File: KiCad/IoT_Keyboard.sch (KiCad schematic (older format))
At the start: 3 parts, among them SW1 SW_Push, U1 Elite-C

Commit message: Update IoT_Keyboard.sch
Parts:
- added C?: 10uF, symbol Device:C_Small
- added C? (x3): 0.1uF, symbol Device:C_Small
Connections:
- net +5V: now also U1.21 (VCC), C?.1, C?.1, C?.1, C?.1
- net GND: now also C?.2, C?.2, C?.2, C?.2
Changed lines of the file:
@@
 F1 "KeyMatrix.sch" 50
 $EndSheet
+$Comp
+L power:+5V #PWR?
+U 1 1 6035BBF9
+P 5000 3000
+F 0 "#PWR?" H 5000 2850 50  0001 C CNN
+F 1 "+5V" H 5015 3173 50  0000 C CNN
+F 2 "" H 5000 3000 50  0001 C CNN
+F 3 "" H 5000 3000 50  0001 C CNN
+	1    5000 3000
+	1    0    0    -1
+$EndComp
+Wire Wire Line
+	4200 3350 4850 3350
+Wire Wire Line
+	4850 3350 4850 3000
+Wire Wire Line
+	4850 3000 5000 3000
+$Comp
+L Device:C_Small C?
+U 1 1 6035F335
+P 1900 3950
+F 0 "C?" H 1992 3996 50  0000 L CNN
+F 1 "10uF" H 1992 3905 50  0000 L CNN
+F 2 "" H 1900 3950 50  0001 C CNN
+F 3 "~" H 1900 3950 50  0001 C CNN
+	1    1900 3950
+	1    0    0    -1
+$EndComp
+$Comp
+L Device:C_Small C?
+U 1 1 60360918
+P 1600 3950
+F 0 "C?" H 1692 3996 50  0000 L CNN
+F 1 "0.1uF" H 1692 3905 50  0000 L CNN
+F 2 "" H 1600 3950 50  0001 C CNN
+F 3 "~" H 1600 3950 50  0001 C CNN
+	1    1600 3950
+	1    0    0    -1
+$EndComp
+$Comp
+L Device:C_Small C?
+U 1 1 60360FBB
+P 1300 3950
+F 0 "C?" H 1392 3996 50  0000 L CNN
+F 1 "0.1uF" H 1392 3905 50  0000 L CNN
+F 2 "" H 1300 3950 50  0001 C CNN
+F 3 "~" H 1300 3950 50  0001 C CNN
+	1    1300 3950
+	1    0    0    -1
+$EndComp
+$Comp
+L Device:C_Small C?
+U 1 1 603612C2
+P 1000 3950
+F 0 "C?" H 1092 3996 50  0000 L CNN
+F 1 "0.1uF" H 1092 3905 50  0000 L CNN
+F 2 "" H 1000 3950 50  0001 C CNN
+F 3 "~" H 1000 3950 50  0001 C CNN
+	1    1000 3950
+	1    0    0    -1
+$EndComp
+Wire Wire Line
+	1000 4050 1300 4050
+Wire Wire Line
+	1300 4050 1450 4050
+Connection ~ 1300 4050
+Wire Wire Line
+	1600 4050 1900 4050
+Connection ~ 1600 4050
+Wire Wire Line
+	1900 3850 1900 3800
+Wire Wire Line
+	1900 3800 1600 3800
+Wire Wire Line
+	1600 3800 1600 3850
+Wire Wire Line
+	1600 3800 1450 3800
+Wire Wire Line
+	1300 3800 1300 3850
+Connection ~ 1600 3800
+Wire Wire Line
+	1300 3800 1000 3800
+Wire Wire Line
+	1000 3800 1000 3850
+Connection ~ 1300 3800
+$Comp
+L power:+5V #PWR?
+U 1 1 60364907
+P 1450 3700
+F 0 "#PWR?" H 1450 3550 50  0001 C CNN
+F 1 "+5V" H 1465 3873 50  0000 C CNN
+F 2 "" H 1450 3700 50  0001 C CNN
+F 3 "" H 1450 3700 50  0001 C CNN
+	1    1450 3700
+	1    0    0    -1
+$EndComp
+$Comp
+L power:GND #PWR?
+U 1 1 603653B9
+P 1450 4150
+F 0 "#PWR?" H 1450 3900 50  0001 C CNN
+F 1 "GND" H 1455 3977 50  0000 C CNN
+F 2 "" H 1450 4150 50  0001 C CNN
+F 3 "" H 1450 4150 50  0001 C CNN
+	1    1450 4150
+	1    0    0    -1
+$EndComp
+Wire Wire Line
+	1450 3800 1450 3700
+Connection ~ 1450 3800
+Wire Wire Line
+	1450 3800 1300 3800
+Wire Wire Line
+	1450 4050 1450 4150
+Connection ~ 1450 4050
+Wire Wire Line
+	1450 4050 1600 4050
 $EndSCHEMATC

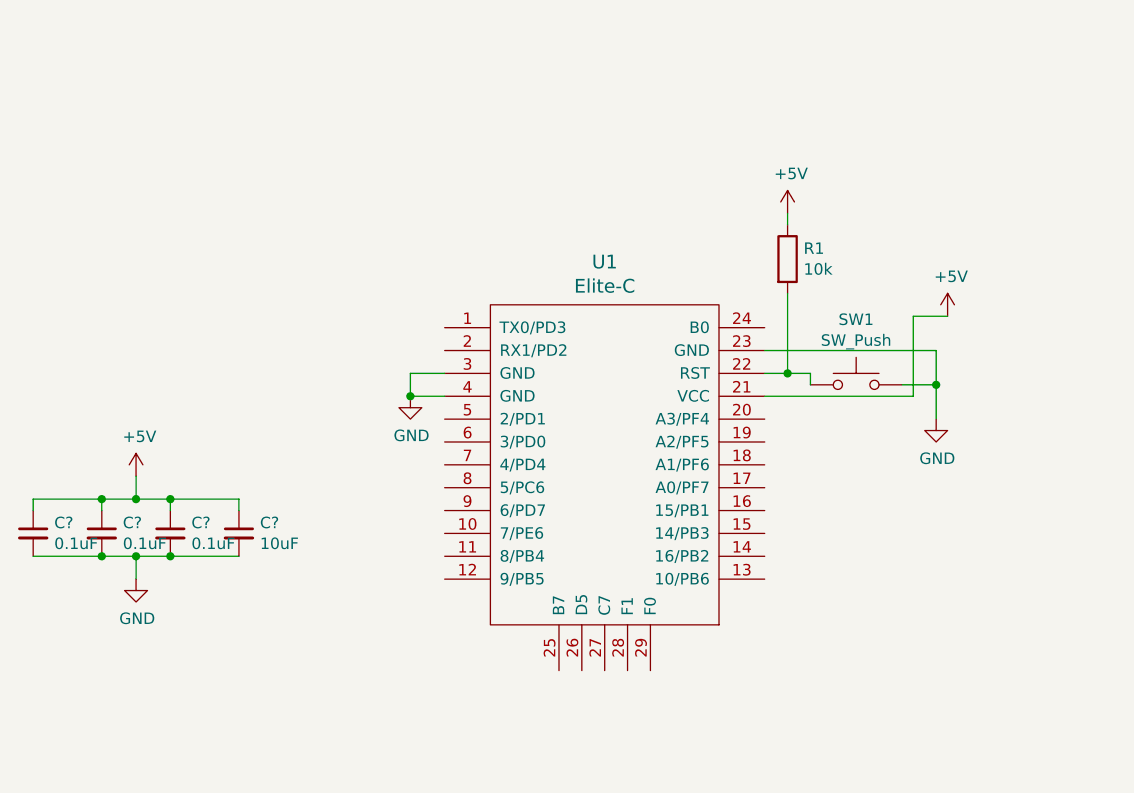
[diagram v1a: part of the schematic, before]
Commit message: Wired Rows/Cols of Switches. Created Physical PCB.
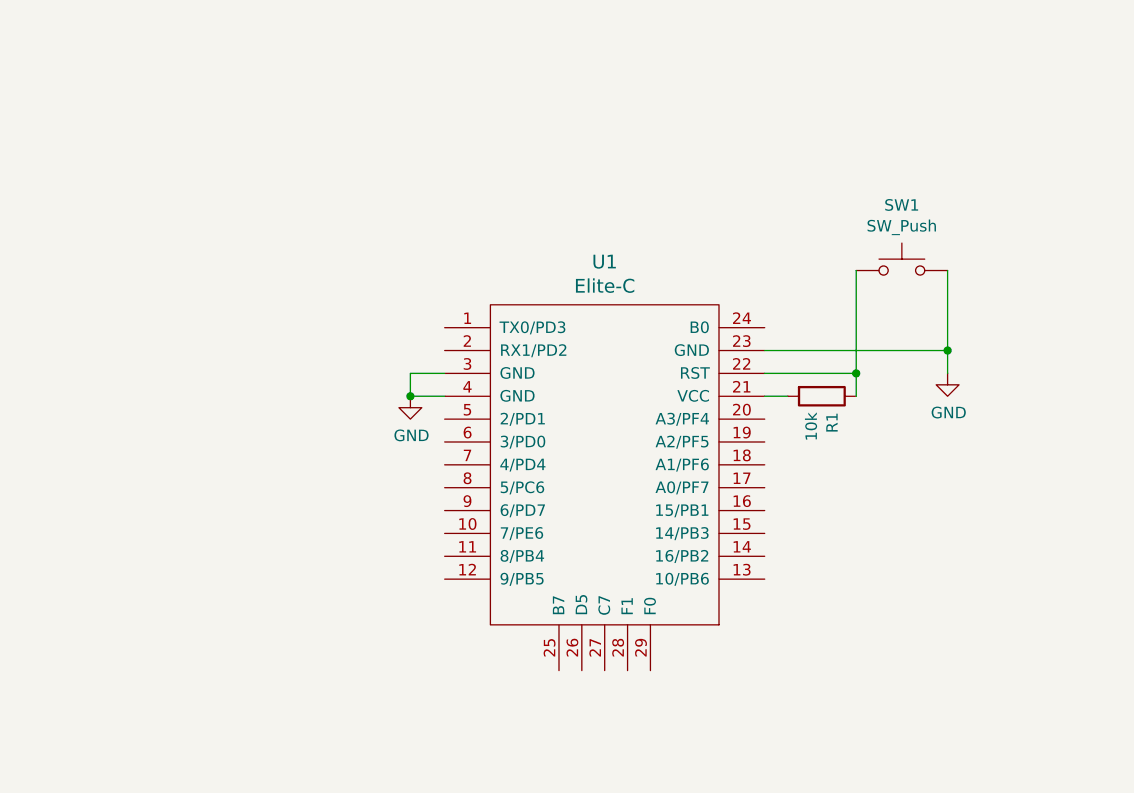
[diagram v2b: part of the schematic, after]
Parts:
- removed C?: 10uF, symbol Device:C_Small
- removed C? (x3): 0.1uF, symbol Device:C_Small
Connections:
- net at SW1.1, U1.22 (RST): now also R1.1; no longer R1.2
- net +5V: no longer names the net of U1.21 (VCC)
- net +5V: now also R1.2; no longer R1.1
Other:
- moved on the sheet: R1, SW1
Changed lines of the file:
@@
 Wire Wire Line
 	2650 3250 2650 3350
-Wire Wire Line
-	4200 3250 4300 3250
-Wire Wire Line
-	4400 3250 4400 3300
 $Comp
 L power:GND #PWR0102
 U 1 1 60210421
-P 4950 3450
-F 0 "#PWR0102" H 4950 3200 50  0001 C CNN
-F 1 "GND" H 4955 3277 50  0000 C CNN
-F 2 "" H 4950 3450 50  0001 C CNN
-F 3 "" H 4950 3450 50  0001 C CNN
-	1    4950 3450
-	1    0    0    -1
-$EndComp
-Wire Wire Line
-	4300 3250 4300 2900
-Connection ~ 4300 3250
-Wire Wire Line
-	4300 3250 4400 3250
-$Comp
-L power:+5V #PWR0103
-U 1 1 602126FC
-P 4300 2550
-F 0 "#PWR0103" H 4300 2400 50  0001 C CNN
-F 1 "+5V" H 4315 2723 50  0000 C CNN
-F 2 "" H 4300 2550 50  0001 C CNN
-F 3 "" H 4300 2550 50  0001 C CNN
-	1    4300 2550
-	1    0    0    -1
-$EndComp
-Wire Wire Line
-	4300 2600 4300 2550
-$Comp
-L Switch:SW_Push SW1
-U 1 1 6020EE71
-P 4600 3300
-F 0 "SW1" H 4600 3585 50  0000 C CNN
-F 1 "SW_Push" H 4600 3494 50  0000 C CNN
-F 2 "Keebio:SW_SPST_3x3" H 4600 3500 50  0001 C CNN
-F 3 "~" H 4600 3500 50  0001 C CNN
-	1    4600 3300
+P 5000 3250
+F 0 "#PWR0102" H 5000 3000 50  0001 C CNN
+F 1 "GND" H 5005 3077 50  0000 C CNN
+F 2 "" H 5000 3250 50  0001 C CNN
+F 3 "" H 5000 3250 50  0001 C CNN
+	1    5000 3250
 	1    0    0    -1
 $EndComp
@@
 L Device:R R1
 U 1 1 60211719
-P 4300 2750
-F 0 "R1" H 4370 2796 50  0000 L CNN
-F 1 "10k" H 4370 2705 50  0000 L CNN
-F 2 "Resistor_SMD:R_0805_2012Metric" V 4230 2750 50  0001 C CNN
-F 3 "~" H 4300 2750 50  0001 C CNN
-	1    4300 2750
-	1    0    0    -1
+P 4450 3350
+F 0 "R1" H 4520 3396 50  0000 L CNN
+F 1 "10k" H 4520 3305 50  0000 L CNN
+F 2 "Resistor_SMD:R_0805_2012Metric" V 4380 3350 50  0001 C CNN
+F 3 "~" H 4450 3350 50  0001 C CNN
+	1    4450 3350
+	0    1    1    0
 $EndComp
 $Comp
@@
 	1    0    0    -1
 $EndComp
-Wire Wire Line
-	4200 3150 4950 3150
-Wire Wire Line
-	4950 3150 4950 3300
-Wire Wire Line
-	4800 3300 4950 3300
-Connection ~ 4950 3300
-Wire Wire Line
-	4950 3300 4950 3450
 $Sheet
 S 12000 0    11700 8250
@@
 $EndSheet
 $Comp
-L power:+5V #PWR?
-U 1 1 6035BBF9
-P 5000 3000
-F 0 "#PWR?" H 5000 2850 50  0001 C CNN
-F 1 "+5V" H 5015 3173 50  0000 C CNN
-F 2 "" H 5000 3000 50  0001 C CNN
-F 3 "" H 5000 3000 50  0001 C CNN
-	1    5000 3000
+L Switch:SW_Push SW1
+U 1 1 6020EE71
+P 4800 2800
+F 0 "SW1" H 4800 3085 50  0000 C CNN
+F 1 "SW_Push" H 4800 2994 50  0000 C CNN
+F 2 "Keebio:SW_SPST_3x3" H 4800 3000 50  0001 C CNN
+F 3 "~" H 4800 3000 50  0001 C CNN
+	1    4800 2800
 	1    0    0    -1
 $EndComp
 Wire Wire Line
-	4200 3350 4850 3350
+	4200 3350 4300 3350
 Wire Wire Line
-	4850 3350 4850 3000
+	4600 3350 4600 3250
 Wire Wire Line
-	4850 3000 5000 3000
-$Comp
-L Device:C_Small C?
-U 1 1 6035F335
-P 1900 3950
-F 0 "C?" H 1992 3996 50  0000 L CNN
-F 1 "10uF" H 1992 3905 50  0000 L CNN
-F 2 "" H 1900 3950 50  0001 C CNN
-F 3 "~" H 1900 3950 50  0001 C CNN
-	1    1900 3950
-	1    0    0    -1
-$EndComp
-$Comp
-L Device:C_Small C?
-U 1 1 60360918
-P 1600 3950
-F 0 "C?" H 1692 3996 50  0000 L CNN
-F 1 "0.1uF" H 1692 3905 50  0000 L CNN
-F 2 "" H 1600 3950 50  0001 C CNN
-F 3 "~" H 1600 3950 50  0001 C CNN
-	1    1600 3950
-	1    0    0    -1
-$EndComp
-$Comp
-L Device:C_Small C?
-U 1 1 60360FBB
-P 1300 3950
-F 0 "C?" H 1392 3996 50  0000 L CNN
-F 1 "0.1uF" H 1392 3905 50  0000 L CNN
-F 2 "" H 1300 3950 50  0001 C CNN
-F 3 "~" H 1300 3950 50  0001 C CNN
-	1    1300 3950
-	1    0    0    -1
-$EndComp
-$Comp
-L Device:C_Small C?
-U 1 1 603612C2
-P 1000 3950
-F 0 "C?" H 1092 3996 50  0000 L CNN
-F 1 "0.1uF" H 1092 3905 50  0000 L CNN
-F 2 "" H 1000 3950 50  0001 C CNN
-F 3 "~" H 1000 3950 50  0001 C CNN
-	1    1000 3950
-	1    0    0    -1
-$EndComp
+	4200 3250 4600 3250
+Connection ~ 4600 3250
+Connection ~ 5000 3150
 Wire Wire Line
-	1000 4050 1300 4050
+	5000 3150 5000 3250
 Wire Wire Line
-	1300 4050 1450 4050
-Connection ~ 1300 4050
+	4200 3150 5000 3150
 Wire Wire Line
-	1600 4050 1900 4050
-Connection ~ 1600 4050
+	5000 2800 5000 3150
 Wire Wire Line
-	1900 3850 1900 3800
-Wire Wire Line
-	1900 3800 1600 3800
-Wire Wire Line
-	1600 3800 1600 3850
-Wire Wire Line
-	1600 3800 1450 3800
-Wire Wire Line
-	1300 3800 1300 3850
-Connection ~ 1600 3800
-Wire Wire Line
-	1300 3800 1000 3800
-Wire Wire Line
-	1000 3800 1000 3850
-Connection ~ 1300 3800
-$Comp
-L power:+5V #PWR?
-U 1 1 60364907
-P 1450 3700
-F 0 "#PWR?" H 1450 3550 50  0001 C CNN
-F 1 "+5V" H 1465 3873 50  0000 C CNN
-F 2 "" H 1450 3700 50  0001 C CNN
-F 3 "" H 1450 3700 50  0001 C CNN
-	1    1450 3700
-	1    0    0    -1
-$EndComp
-$Comp
-L power:GND #PWR?
-U 1 1 603653B9
-P 1450 4150
-F 0 "#PWR?" H 1450 3900 50  0001 C CNN
-F 1 "GND" H 1455 3977 50  0000 C CNN
-F 2 "" H 1450 4150 50  0001 C CNN
-F 3 "" H 1450 4150 50  0001 C CNN
-	1    1450 4150
-	1    0    0    -1
-$EndComp
-Wire Wire Line
-	1450 3800 1450 3700
-Connection ~ 1450 3800
-Wire Wire Line
-	1450 3800 1300 3800
-Wire Wire Line
-	1450 4050 1450 4150
-Connection ~ 1450 4050
-Wire Wire Line
-	1450 4050 1600 4050
+	4600 3250 4600 2800
 $EndSCHEMATC

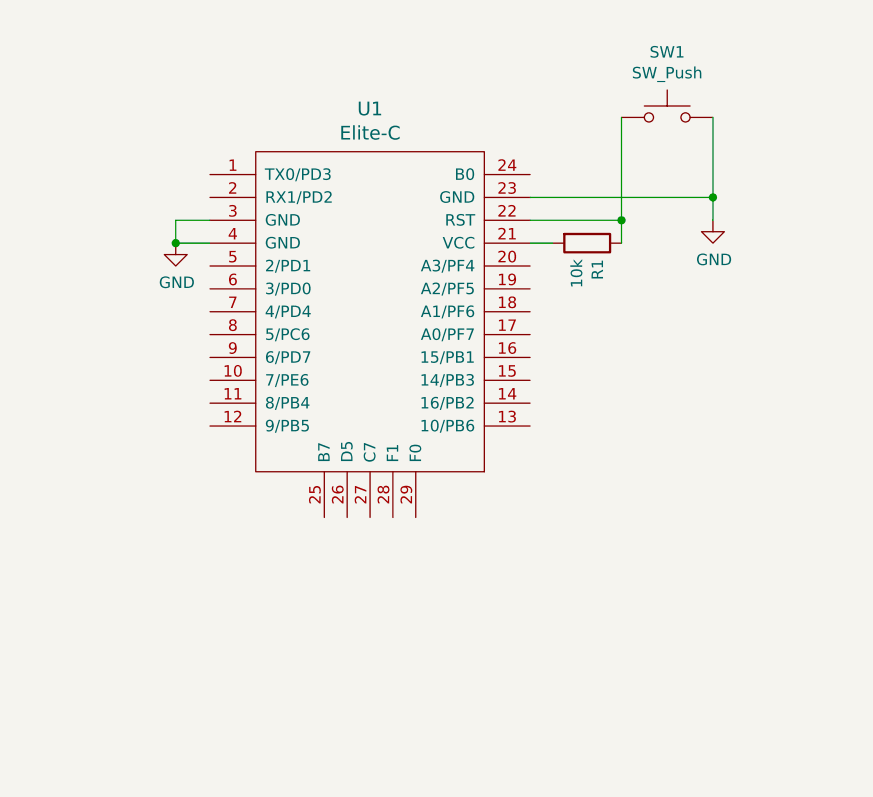
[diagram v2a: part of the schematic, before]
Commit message: Routed rows and columsn to microcontroller with Daniel
 :)
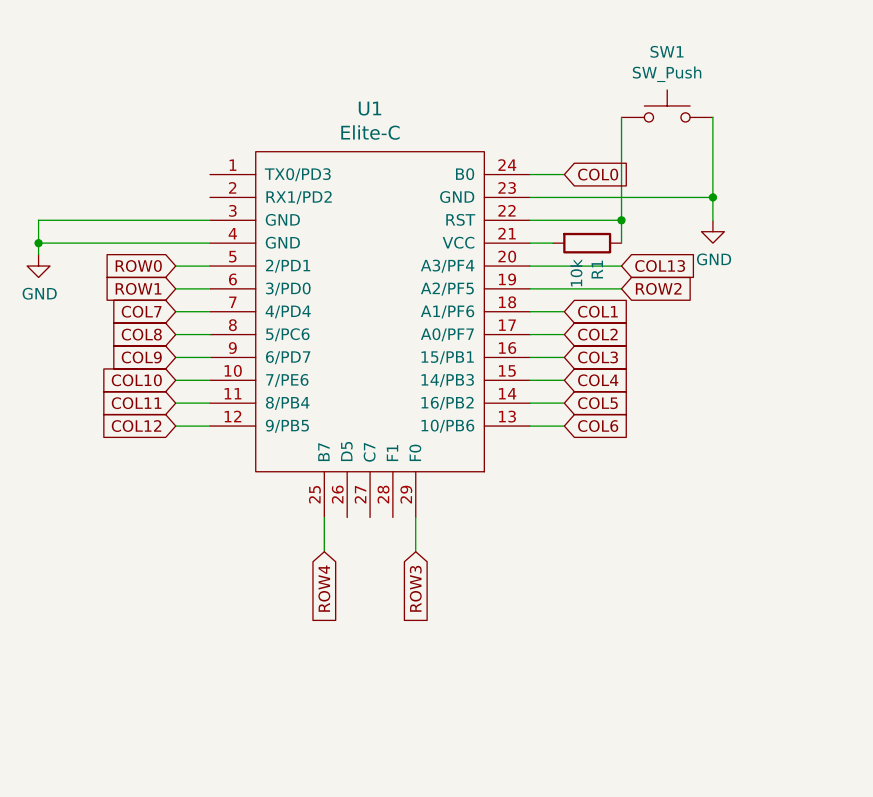
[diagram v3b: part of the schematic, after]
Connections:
- net COL10: now reaches U1.10 (7/PE6)
- net COL11: now reaches U1.11 (8/PB4)
- net COL12: now reaches U1.12 (9/PB5)
- net COL6: now reaches U1.13 (10/PB6)
- net COL5: now reaches U1.14 (16/PB2)
- net COL4: now reaches U1.15 (14/PB3)
- net COL3: now reaches U1.16 (15/PB1)
- net COL2: now reaches U1.17 (A0/PF7)
- net COL1: now reaches U1.18 (A1/PF6)
- net ROW2: now reaches U1.19 (A2/PF5)
- net COL13: now reaches U1.20 (A3/PF4)
- net COL0: now reaches U1.24 (B0)
- net ROW4: now reaches U1.25 (B7)
- net ROW3: now reaches U1.29 (F0)
- net ROW0: now reaches U1.5 (2/PD1)
- net ROW1: now reaches U1.6 (3/PD0)
- net COL7: now reaches U1.7 (4/PD4)
- net COL8: now reaches U1.8 (5/PC6)
- net COL9: now reaches U1.9 (6/PD7)
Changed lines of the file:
@@
 L power:GND #PWR0101
 U 1 1 601FE667
-P 2650 3350
-F 0 "#PWR0101" H 2650 3100 50  0001 C CNN
-F 1 "GND" H 2655 3177 50  0000 C CNN
-F 2 "" H 2650 3350 50  0001 C CNN
-F 3 "" H 2650 3350 50  0001 C CNN
-	1    2650 3350
+P 2050 3400
+F 0 "#PWR0101" H 2050 3150 50  0001 C CNN
+F 1 "GND" H 2055 3227 50  0000 C CNN
+F 2 "" H 2050 3400 50  0001 C CNN
+F 3 "" H 2050 3400 50  0001 C CNN
+	1    2050 3400
 	1    0    0    -1
 $EndComp
-Wire Wire Line
-	2800 3350 2650 3350
-Connection ~ 2650 3350
-Wire Wire Line
-	2800 3250 2650 3250
-Wire Wire Line
-	2650 3250 2650 3350
 $Comp
 L power:GND #PWR0102
@@
 Wire Wire Line
 	4600 3250 4600 2800
+Text GLabel 4350 3050 2    50   Input ~ 0
+COL0
+Wire Wire Line
+	4200 3050 4350 3050
+Text GLabel 4350 3650 2    50   Input ~ 0
+COL1
+Text GLabel 4350 3750 2    50   Input ~ 0
+COL2
+Text GLabel 4350 3850 2    50   Input ~ 0
+COL3
+Text GLabel 4350 3950 2    50   Input ~ 0
+COL4
+Text GLabel 4350 4050 2    50   Input ~ 0
+COL5
+Wire Wire Line
+	4200 3650 4350 3650
+Text GLabel 4350 4150 2    50   Input ~ 0
+COL6
+Wire Wire Line
+	4200 3750 4350 3750
+Wire Wire Line
+	4200 3850 4350 3850
+Wire Wire Line
+	4200 3950 4350 3950
+Wire Wire Line
+	4200 4050 4350 4050
+Wire Wire Line
+	4200 4150 4350 4150
+Text GLabel 2650 3650 0    50   Input ~ 0
+COL7
+Text GLabel 2650 3750 0    50   Input ~ 0
+COL8
+Text GLabel 2650 3850 0    50   Input ~ 0
+COL9
+Text GLabel 2650 3950 0    50   Input ~ 0
+COL10
+Text GLabel 2650 4050 0    50   Input ~ 0
+COL11
+Text GLabel 2650 4150 0    50   Input ~ 0
+COL12
+Wire Wire Line
+	2650 3650 2800 3650
+Wire Wire Line
+	2650 3750 2800 3750
+Wire Wire Line
+	2650 3850 2800 3850
+Wire Wire Line
+	2650 3950 2800 3950
+Wire Wire Line
+	2650 4050 2800 4050
+Wire Wire Line
+	2650 4150 2800 4150
+Text GLabel 4600 3450 2    50   Input ~ 0
+COL13
+Wire Wire Line
+	2050 3250 2800 3250
+Wire Wire Line
+	2050 3250 2050 3350
+Wire Wire Line
+	2050 3350 2800 3350
+Connection ~ 2050 3350
+Wire Wire Line
+	2050 3350 2050 3400
+Wire Wire Line
+	4200 3450 4600 3450
+Wire Wire Line
+	4200 3550 4600 3550
+Wire Wire Line
+	2650 3450 2800 3450
+Wire Wire Line
+	2650 3550 2800 3550
+Wire Wire Line
+	3300 4550 3300 4700
+Wire Wire Line
+	3700 4550 3700 4700
+Text GLabel 2650 3450 0    50   Input ~ 0
+ROW0
+Text GLabel 2650 3550 0    50   Input ~ 0
+ROW1
+Text GLabel 4600 3550 2    50   Input ~ 0
+ROW2
+Text GLabel 3300 4700 3    50   Input ~ 0
+ROW4
+Text GLabel 3700 4700 3    50   Input ~ 0
+ROW3
 $EndSCHEMATC
